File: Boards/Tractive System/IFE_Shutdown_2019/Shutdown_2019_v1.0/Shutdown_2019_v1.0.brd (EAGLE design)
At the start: 88.9 x 76.2 mm, 94 parts, among them Q1 DMN6140L-7, Q11 DMP3099L-7, Q12 IRLML6346PBF, Q13 IRLML6346PBF, Q14 IRLML6346PBF, Q15 DMP3099L-7, Q16 DMN6140L-7, Q17 IRLML6346PBF, Q2 DMN6140L-7, Q3 DMN6140L-7, Q4 DMN6140L-7, Q5 DMN6140L-7, Q6 DMP3099L-7, Q7 DMN6140L-7, Q8 DMN6140L-7, Q9 DMN6140L-7, U1 STM32F103CBT6

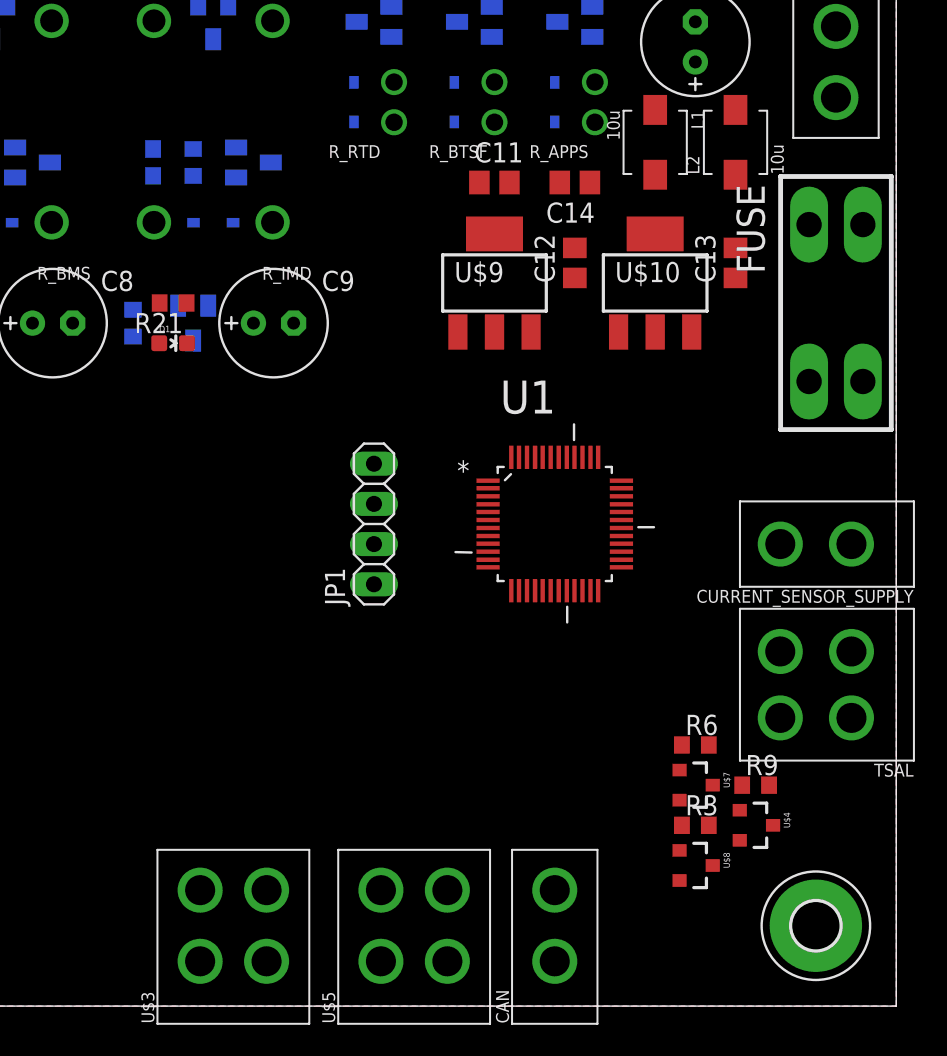
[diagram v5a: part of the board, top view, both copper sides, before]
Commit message: added CAN circuit and DEBUG headder
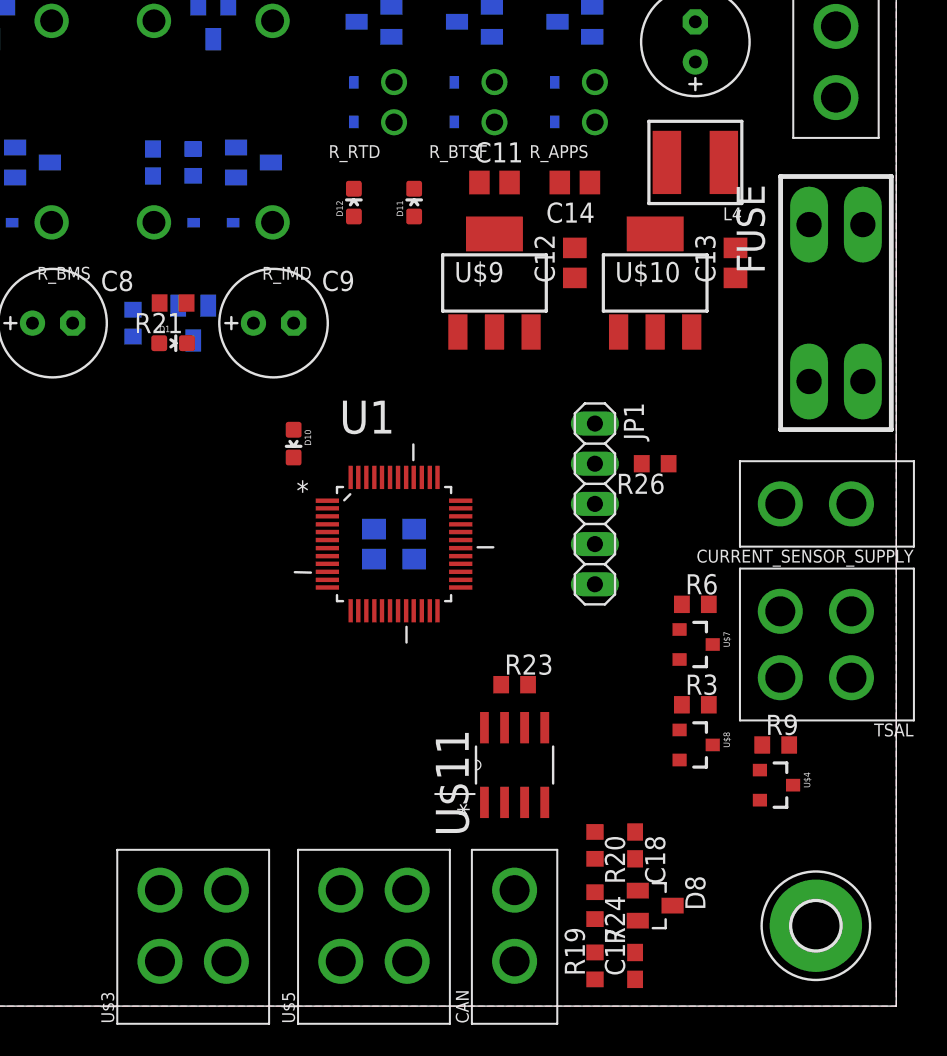
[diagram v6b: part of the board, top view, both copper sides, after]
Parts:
- removed L1, L2: 10u, SparkFun-Passives:INDUCTOR-SRP4020
- added C15, C19: 1u, rcl:C0805
- added C17, C18: 560p, rcl:C0603
- added D10: RED, SparkFun-LED:LED-0603
- added D11, D12: GREEN, SparkFun-LED:LED-0603
- added D8: PESD1, diode:SOT23
- added L4: 10u, microbuilder:INDUCTOR_5X5MM_NR5040_NOTHERMALS
- added R19, R20: 100, rcl:R0603
- added R23: 4.7k, rcl:R0603
- added R24: 120, rcl:R0603
- added R26: 10k, rcl:R0603
- added U$11: MCP2551, Microchip_By_element14_Batch_1:SOIC127P600X175-8N
- JP1: device Headers_IFE:1X04 -> Headers_IFE:1X05
- moved JP1 14.0 mm to (69.8, 31.8), turned to 270 degrees
- moved U1 10.2 mm to (57.1, 29.2)
- moved U$7 8.89 mm to (76.2, 22.9)
- moved R6 8.89 mm to (76.2, 25.4)
- moved R3 7.62 mm to (76.2, 19.1)
- moved U$8 7.62 mm to (76.2, 16.5)
- moved R9 2.84 mm to (81.3, 16.5)
- moved U$4 2.84 mm to (81.3, 14.0)
- moved CAN 2.54 mm to (64.8, 5.08)
- moved CURRENT_SENSOR_SUPPLY 2.54 mm to (83.8, 31.8)
- moved TSAL 2.54 mm to (83.8, 22.9)
- moved U$3 2.54 mm to (44.5, 5.08)
- moved U$5 2.54 mm to (55.9, 5.08)
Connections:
- removed net N$5: C10.+, L1.P$1, L2.P$2
- removed net VDD_2: U1.36
- removed net VDD_3: U1.48
- new net !RST: JP1.2, R26.2, U1.7
- new net N$14: C17.1, R19.1
- new net N$17: C18.1, R20.1
- new net N$18: R23.1, U$11.8
- new net RXCAN: U$11.4
- new net SWDCLK: JP1.4
- new net SWDIO: JP1.3
- new net TXCAN: U$11.1
- net +12V: now also C10.+, L4.P$2; no longer L1.P$2
- net +3V3: now also C15.1, C19.1, JP1.1, R26.1, U1.24, U1.36, U1.48
- net +5V: now also U$11.3
- net CANH: now also D8.1, R20.2, R24.2, U$11.7
- net CANL: now also D8.2, R19.2, R24.1, U$11.6
- net GND: now also C15.2, C17.2, C18.2, C19.2, D8.3, JP1.5, R23.2, U$11.2, U1.20, U1.23, U1.35, U1.44, U1.47, U1.8
- net N$6: now also L4.P$1; no longer L2.P$1

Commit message: Added digital POT for TC
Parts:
- added R27: 10k, rcl:R0603
- added U$12: MCP4018, MICROCHIP:SOT23-6
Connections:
- new net DEBUG: D10.C, U1.2
- new net N$19: D10.A, R27.2
- net +3V3: now also R27.1
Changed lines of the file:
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@@
 <attribute name="PROD_ID" value="DIO-00821" x="54.61" y="50.8" size="1.778" layer="27" display="off"/>
+</element>
+<element name="U$12" library="MICROCHIP" package="SOT23-6" value="MCP4018" x="35.56" y="8.89" rot="R270"/>
+<element name="R27" library="rcl" library_urn="urn:adsk.eagle:library:334" package="R0603" package3d_urn="urn:adsk.eagle:package:23555/2" value="10k" x="48.26" y="35.56" rot="R90">
+<attribute name="SPICEPREFIX" value="R" x="48.26" y="35.56" size="1.778" layer="27" rot="R90" display="off"/>
 </element>
 </elements>
@@
 <contactref element="C19" pad="1"/>
 <contactref element="R26" pad="1"/>
+<contactref element="R27" pad="1"/>
 <wire x1="62.55" y1="52.07" x2="63.5" y2="48.819" width="0" layer="19" extent="1-1"/>
 <wire x1="63.5" y1="42.6212" x2="63.5" y2="48.819" width="0" layer="19" extent="1-1"/>
 <wire x1="69.85" y1="36.83" x2="63.5" y2="42.6212" width="0" layer="19" extent="1-1"/>
+<wire x1="74.51" y1="34.29" x2="69.85" y2="36.83" width="0" layer="19" extent="1-1"/>
 <wire x1="61.3664" y1="31.9532" x2="69.85" y2="36.83" width="0" layer="19" extent="1-1"/>
-<wire x1="58.42" y1="30.16" x2="61.3664" y2="31.9532" width="0" layer="19" extent="1-1"/>
-<wire x1="55.88" y1="28.26" x2="58.42" y2="30.16" width="0" layer="19" extent="1-1"/>
-<wire x1="59.8932" y1="24.9936" x2="58.42" y2="30.16" width="0" layer="19" extent="1-1"/>
-<wire x1="54.4068" y1="33.4264" x2="55.88" y2="28.26" width="0" layer="19" extent="1-1"/>
-<wire x1="74.51" y1="34.29" x2="54.4068" y2="33.4264" width="0" layer="19" extent="1-1"/>
-<wire x1="40.64" y1="42.33" x2="74.51" y2="34.29" width="0" layer="19" extent="1-16"/>
+<wire x1="58.42" y1="30.16" x2="61.3664" y2="31.9532" width="0" layer="19" extent="1-16"/>
+<wire x1="55.88" y1="28.26" x2="58.42" y2="30.16" width="0" layer="19" extent="16-16"/>
+<wire x1="54.4068" y1="33.4264" x2="58.42" y2="30.16" width="0" layer="19" extent="1-16"/>
+<wire x1="59.8932" y1="24.9936" x2="55.88" y2="28.26" width="0" layer="19" extent="1-16"/>
+<wire x1="40.64" y1="42.33" x2="54.4068" y2="33.4264" width="0" layer="19" extent="1-16"/>
 <wire x1="26.67" y1="42.33" x2="40.64" y2="42.33" width="0" layer="19" extent="16-16"/>
 <wire x1="12.7" y1="42.33" x2="26.67" y2="42.33" width="0" layer="19" extent="16-16"/>
+<wire x1="48.26" y1="34.71" x2="12.7" y2="42.33" width="0" layer="19" extent="1-16"/>
 </signal>
 <signal name="FAULT_IMD_STATUS_3_3">
@@
 <wire x1="69.85" y1="11.01" x2="72.39" y2="11.01" width="0" layer="19" extent="1-1"/>
 </signal>
+<signal name="DEBUG">
+<contactref element="U1" pad="2"/>
+<contactref element="D10" pad="C"/>
+<wire x1="52.9336" y1="31.4706" x2="50.8" y2="34.683" width="0" layer="19" extent="1-1"/>
+</signal>
+<signal name="N$19">
+<contactref element="D10" pad="A"/>
+<contactref element="R27" pad="2"/>
+<wire x1="48.26" y1="36.41" x2="50.8" y2="36.437" width="0" layer="19" extent="1-1"/>
+</signal>
 </signals>

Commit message: starting to connect subsystems
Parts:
- removed R23: 4.7k, rcl:R0603
- U$11: value MCP2551 -> MCP2562; device Microchip_By_element14_Batch_1:SOIC127P600X175-8N -> MICROCHIP:SOIC8
- turned U$11 to 180 degrees
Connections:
- removed net N$18: R23.1, U$11.8
- removed net RXCAN: U$11.4
- removed net SWDCLK: JP1.4
- removed net TXCAN: U$11.1
- new net CAN_RX: U$11.4, U1.45
- new net CAN_SBTY: U1.43
- new net CAN_STBY: U$11.8
- new net CAN_TX: U$11.1, U1.46
- new net SPI1_MISO: U1.16
- new net SPI1_MOSI: U1.17
- new net SPI1_NSS: U1.14
- new net SPI1_SCK: U1.15
- new net SWCLK: JP1.4, U1.37
- net +3V3: now also U$11.5
- net FAULT_BMS_STATUS_3_3: now also U1.12
- net FAULT_BSPD_STATUS_3_3: now also U1.11
- net FAULT_IMD_STATUS_3_3: now also U1.13
- net GND: no longer R23.2
- net SWDIO: now also U1.34
